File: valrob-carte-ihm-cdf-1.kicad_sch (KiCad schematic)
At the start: 42 parts, among them J1 USB_C_Receptacle_USB2.0_14P, J2 Conn_01x02, J3 Conn_01x02, J4 Conn_01x04_Pin, J5 Conn_01x04_Pin, J9 Conn_01x04_Pin, SW1 SW_Push, SW2 SW_Push, SW3 SW_DIP_x04, U1 TLV75733PDBV, U2 USBLC6-2SC6, U3 ESP32-S3-WROOM-1, U5 HS96L03W2C03

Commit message: schem: connect i2c to MCU
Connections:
- net SCL: now also U3.12 (GPIO8/TOUCH8/ADC1_CH7/SUBSPICS1)
- net SDA: now also U3.17 (GPIO9/TOUCH9/ADC1_CH8/FSPIHD/SUBSPIHD)
- no-connect marks 13 -> 11
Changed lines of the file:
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@@
-	)
-	(no_connect
-		(at 246.38 95.25)
-	)
-	(no_connect
-		(at 246.38 92.71)
 	)
 	(no_connect
@@
 	(wire
 		(pts
+			(xy 250.19 95.25) (xy 246.38 95.25)
+		)
+		(stroke
+			(width 0)
+			(type default)
+		)
+	)
+	(wire
+		(pts
 			(xy 50.8 171.45) (xy 50.8 168.91)
 		)
@@
 	(wire
 		(pts
+			(xy 250.19 92.71) (xy 246.38 92.71)
+		)
+		(stroke
+			(width 0)
+			(type default)
+		)
+	)
+	(wire
+		(pts
 			(xy 200.66 133.35) (xy 200.66 135.89)
 		)
@@
 			(width 0)
 			(type default)
+		)
+	)
+	(label "SDA"
+		(at 250.19 95.25 180)
+		(effects
+			(font
+				(size 1.27 1.27)
+			)
+			(justify right bottom)
 		)
 	)
@@
 		(effects
 			(font
+				(size 1.27 1.27)
+			)
+			(justify right bottom)
+		)
+	)
+	(label "SCL"
+		(at 250.19 92.71 180)
+		(effects
+			(font

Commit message: schem: run and fix ERC
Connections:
- net RGB_LEDS: now also U3.15 (GPIO3/TOUCH3/ADC1_CH2)
- no-connect marks 11 -> 10
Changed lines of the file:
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@@
-	)
-	(no_connect
-		(at 246.38 80.01)
 	)
 	(no_connect
@@
 		(pts
 			(xy 71.12 140.97) (xy 71.12 142.24)
+		)
+		(stroke
+			(width 0)
+			(type default)
+		)
+	)
+	(wire
+		(pts
+			(xy 256.54 80.01) (xy 246.38 80.01)
 		)
 		(stroke
@@
 		(effects
 			(font
+				(size 1.27 1.27)
+			)
+			(justify right bottom)
+		)
+	)
+	(label "RGB_LEDS"
+		(at 256.54 80.01 180)
+		(effects
+			(font

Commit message: schem: add title
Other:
- company: (none) -> Valrobotik
- title: (none) -> Carte IHM CDF 1
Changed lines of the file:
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@@
 	(generator_version "9.0")
 	(paper "A4")
+	(title_block
+		(title "Carte IHM CDF 1")
+		(date "2025-11-24")
+		(rev "01")
+		(company "Valrobotik")
+	)
 	(rectangle
 		(start 15.24 118.11)

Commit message: schem: reannotate
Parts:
- renumbered D12 to D1, D16 to D2, D13 to D3, D1 to D4, D14 to D5, D2 to D6, D3 to D7, D4 to D8, D5 to D9, J9 to J4, J4 to J6, R6 to R5, R5 to R6, TP6 to TP1, TP7 to TP2, U5 to U3, U3 to U4

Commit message: schem: assign footprints
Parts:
- C1, C2: footprint (none) -> Capacitor_SMD:C_0603_1608Metric
- C4: footprint Capacitor_SMD:C_0603_1608Metric -> Capacitor_SMD:C_0402_1005Metric; Basic Y -> (none); JLCPCB Part # C14663 -> (none); Manufacturer YAGEO -> (none); Manufacturer Part Number CC0603KRX7R9BB104 -> (none)
- C5: footprint Capacitor_SMD:C_0603_1608Metric -> Capacitor_SMD:C_0402_1005Metric; JLCPCB Part # C15849 -> (none); Manufacturer Samsung Electro-Mechanics -> (none)
- C6: footprint Capacitor_SMD:C_0805_2012Metric -> Capacitor_SMD:C_0603_1608Metric; Basic Y -> (none); JLCPCB Part # C45783 -> (none); Manufacturer Samsung Electro-Mechanics -> (none); Manufacturer Part Number CL21A226MAQNNNE -> (none)
- C7: footprint Capacitor_SMD:C_0603_1608Metric -> Capacitor_SMD:C_0402_1005Metric; JLCPCB Part # C14663 -> (none); Manufacturer YAGEO -> (none)
- R1, R2, R3: footprint Resistor_SMD:R_0603_1608Metric -> Resistor_SMD:R_0402_1005Metric; JLCPCB Part # C23186 -> (none); Manufacturer Uniroyal Elec -> (none)
- R4: footprint Resistor_SMD:R_0603_1608Metric -> Resistor_SMD:R_0402_1005Metric; JLCPCB Part # C59461 -> (none); Manufacturer Samsung Electro-Mechanics -> (none)
- R5, R6, R7: footprint Resistor_SMD:R_0603_1608Metric -> Resistor_SMD:R_0402_1005Metric; JLCPCB Part # C25804 -> (none); Manufacturer Uniroyal Elec -> (none)
- R8, R9: footprint Resistor_SMD:R_0603_1608Metric -> Resistor_SMD:R_0402_1005Metric; JLCPCB Part # C23345 -> (none); Manufacturer Uniroyal Elec -> (none)
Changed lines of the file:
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@@
 			)
 		)
-		(property "Footprint" "Resistor_SMD:R_0603_1608Metric"
+		(property "Footprint" "Resistor_SMD:R_0402_1005Metric"
 			(at 45.72 170.688 90)
 			(effects
@@
 			)
 		)
-		(property "Manufacturer" "Uniroyal Elec"
+		(property "Manufacturer" ""
 			(at 45.72 168.91 90)
 			(effects
@@
 			)
 		)
-		(property "JLCPCB Part #" "C23186"
+		(property "JLCPCB Part #" ""
 			(at 45.72 168.91 90)
 			(effects
@@
 			)
 		)
-		(property "Footprint" "Resistor_SMD:R_0603_1608Metric"
+		(property "Footprint" "Resistor_SMD:R_0402_1005Metric"
 			(at 259.08 65.532 90)
 			(effects
@@
 			)
 		)
-		(property "JLCPCB Part #" "C23345"
+		(property "JLCPCB Part #" ""
 			(at 259.08 67.31 90)
 			(effects
@@
 			)
 		)
-		(property "Manufacturer" "Uniroyal Elec"
+		(property "Manufacturer" ""
 			(at 259.08 67.31 90)
 			(effects
@@
 			)
 		)
-		(property "Footprint" "Resistor_SMD:R_0603_1608Metric"
+		(property "Footprint" "Resistor_SMD:R_0402_1005Metric"
 			(at 64.77 132.588 90)
 			(effects
@@
 			)
 		)
-		(property "JLCPCB Part #" "C23186"
+		(property "JLCPCB Part #" ""
 			(at 64.77 130.81 90)
 			(effects
@@
 			)
 		)
-		(property "Manufacturer" "Uniroyal Elec"
+		(property "Manufacturer" ""
 			(at 64.77 130.81 90)
 			(effects
@@
 			)
 		)
-		(property "Footprint" ""
+		(property "Footprint" "Capacitor_SMD:C_0603_1608Metric"
 			(at 26.3652 132.08 0)
 			(effects
@@
 			)
 		)
-		(property "Footprint" "Resistor_SMD:R_0603_1608Metric"
+		(property "Footprint" "Resistor_SMD:R_0402_1005Metric"
 			(at 259.08 66.548 90)
 			(effects
@@
 			)
 		)
-		(property "JLCPCB Part #" "C23345"
+		(property "JLCPCB Part #" ""
 			(at 259.08 64.77 90)
 			(effects
@@
 			)
 		)
-		(property "Manufacturer" "Uniroyal Elec"
+		(property "Manufacturer" ""
 			(at 259.08 64.77 90)
 			(effects
@@
 			)
 		)
-		(property "Footprint" "Resistor_SMD:R_0603_1608Metric"
+		(property "Footprint" "Resistor_SMD:R_0402_1005Metric"
 			(at 45.72 168.148 90)
 			(effects
@@
 			)
 		)
-		(property "Manufacturer" "Uniroyal Elec"
+		(property "Manufacturer" ""
 			(at 45.72 166.37 90)
 			(effects
@@
 			)
 		)
-		(property "JLCPCB Part #" "C23186"
+		(property "JLCPCB Part #" ""
 			(at 45.72 166.37 90)
 			(effects
@@
 			)
 		)
-		(property "Footprint" ""
+		(property "Footprint" "Capacitor_SMD:C_0603_1608Metric"
 			(at 56.1848 132.08 0)
 			(effects
@@
 			)
 		)
-		(property "Footprint" "Capacitor_SMD:C_0603_1608Metric"
+		(property "Footprint" "Capacitor_SMD:C_0402_1005Metric"
 			(at 191.4652 44.45 0)
 			(effects
@@
 			)
 		)
-		(property "JLCPCB Part #" "C14663"
+		(property "JLCPCB Part #" ""
 			(at 190.5 40.64 0)
 			(effects
@@
 			)
 		)
-		(property "Manufacturer" "YAGEO"
+		(property "Manufacturer" ""
 			(at 190.5 40.64 0)
 			(effects
@@
 			)
 		)
-		(property "Footprint" "Resistor_SMD:R_0603_1608Metric"
+		(property "Footprint" "Resistor_SMD:R_0402_1005Metric"
 			(at 99.822 147.32 90)
 			(effects
@@
 			)
 		)
-		(property "JLCPCB Part #" "C59461"
+		(property "JLCPCB Part #" ""
 			(at 101.6 147.32 0)
 			(effects
@@
 			)
 		)
-		(property "Manufacturer" "Samsung Electro-Mechanics"
+		(property "Manufacturer" ""
 			(at 101.6 147.32 0)
 			(effects
@@
 			)
 		)
-		(property "Footprint" "Capacitor_SMD:C_0603_1608Metric"
+		(property "Footprint" "Capacitor_SMD:C_0402_1005Metric"
 			(at 140.97 58.1152 0)
 			(effects
@@
 			)
 		)
-		(property "Manufacturer" "Samsung Electro-Mechanics "
+		(property "Manufacturer" ""
 			(at 137.16 57.15 0)
 			(effects
@@
 			)
 		)
-		(property "JLCPCB Part #" "C15849"
+		(property "JLCPCB Part #" ""
 			(at 137.16 57.15 0)
 			(effects
@@
 			)
 		)
-		(property "Footprint" "Resistor_SMD:R_0603_1608Metric"
+		(property "Footprint" "Resistor_SMD:R_0402_1005Metric"
 			(at 257.81 70.612 90)
 			(effects
@@
 			)
 		)
-		(property "Manufacturer" "Uniroyal Elec"
+		(property "Manufacturer" ""
 			(at 257.81 72.39 0)
 			(effects
@@
 			)
 		)
-		(property "JLCPCB Part #" "C25804"
+		(property "JLCPCB Part #" ""
 			(at 257.81 72.39 0)
 			(effects
@@
 			)
 		)
-		(property "Footprint" "Resistor_SMD:R_0603_1608Metric"
+		(property "Footprint" "Resistor_SMD:R_0402_1005Metric"
 			(at 115.57 140.462 90)
 			(effects
@@
 			)
 		)
-		(property "Manufacturer" "Uniroyal Elec"
+		(property "Manufacturer" ""
 			(at 115.57 142.24 0)
 			(effects
@@
 			)
 		)
-		(property "JLCPCB Part #" "C25804"
+		(property "JLCPCB Part #" ""
 			(at 115.57 142.24 0)
 			(effects
@@
 			)
 		)
-		(property "Footprint" "Capacitor_SMD:C_0603_1608Metric"
+		(property "Footprint" "Capacitor_SMD:C_0402_1005Metric"
 			(at 91.7448 151.13 0)
 			(effects
@@
 			)
 		)
-		(property "Basic" "Y"
+		(property "Basic" ""
 			(at 92.71 147.32 0)
 			(effects
@@
 			)
 		)
-		(property "JLCPCB Part #" "C14663"
+		(property "JLCPCB Part #" ""
 			(at 92.71 147.32 0)
 			(effects
@@
 			)
 		)
-		(property "Manufacturer" "YAGEO"
+		(property "Manufacturer" ""
 			(at 92.71 147.32 0)
 			(effects
@@
 			)
 		)
-		(property "Manufacturer Part Number" "CC0603KRX7R9BB104"
+		(property "Manufacturer Part Number" ""
 			(at 92.71 147.32 0)
 			(effects
@@
 			)
 		)
-		(property "Footprint" "Capacitor_SMD:C_0805_2012Metric"
+		(property "Footprint" "Capacitor_SMD:C_0603_1608Metric"
 			(at 181.9148 44.45 0)
 			(effects
@@
 			)
 		)
-		(property "Basic" "Y"
+		(property "Basic" ""
 			(at 182.88 40.64 0)
 			(effects
@@
 			)
 		)
-		(property "JLCPCB Part #" "C45783"
+		(property "JLCPCB Part #" ""
 			(at 182.88 40.64 0)
 			(effects
@@
 			)
 		)
-		(property "Manufacturer" "Samsung Electro-Mechanics "
+		(property "Manufacturer" ""
 			(at 182.88 40.64 0)
 			(effects
@@
 			)
 		)
-		(property "Manufacturer Part Number" "CL21A226MAQNNNE"
+		(property "Manufacturer Part Number" ""
 			(at 182.88 40.64 0)
 			(effects
@@
 			)
 		)
-		(property "Footprint" "Resistor_SMD:R_0603_1608Metric"
+		(property "Footprint" "Resistor_SMD:R_0402_1005Metric"
 			(at 144.018 52.07 90)
 			(effects
@@
 			)
 		)
-		(property "Manufacturer" "Uniroyal Elec"
+		(property "Manufacturer" ""
 			(at 142.24 52.07 0)
 			(effects
@@
 			)
 		)
-		(property "JLCPCB Part #" "C25804"
+		(property "JLCPCB Part #" ""
 			(at 142.24 52.07 0)
 			(effects

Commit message: schem: add part numbers to BOM
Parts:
- C1, C2, C6: Basic (none) -> Y; JLCPCB Part # (none) -> C59461; Manufacturer (none) -> Samsung Electro-Mechanics; Manufacturer Part Number (none) -> CL10A226MQ8NRNC
- C4: Basic (none) -> Y; JLCPCB Part # (none) -> C1525; Manufacturer (none) -> Samsung Electro-Mechanics; Manufacturer Part Number (none) -> CL05B104KO5NNNC
- C5: JLCPCB Part # (none) -> C52923; Manufacturer (none) -> Samsung Electro-Mechanics; Manufacturer Part Number CL10A105KB8NNNC -> CL05A105KA5NQNC
- C7: JLCPCB Part # (none) -> C1525; Manufacturer (none) -> Samsung Electro-Mechanics; Manufacturer Part Number CC0603KRX7R9BB104 -> CL05B104KO5NNNC
- D1, D3, D5: Basic (none) -> X; JLCPCB Part # (none) -> C22371521; Manufacturer (none) -> Worldsemi; Manufacturer Part Number (none) -> WS2812B-HS01/W
- R1, R2, R3: JLCPCB Part # (none) -> C25905; Manufacturer (none) -> Uniroyal Elec; Manufacturer Part Number 0603WAF5101T5E -> 0402WGF5101TCE
- R4: footprint Resistor_SMD:R_0402_1005Metric -> Resistor_SMD:R_0603_1608Metric; JLCPCB Part # (none) -> C4177; Manufacturer (none) -> Uniroyal Elec; Manufacturer Part Number CL10A226MQ8NRNC -> 0603WAF1801T5E
- R5, R6, R7: JLCPCB Part # (none) -> C25744; Manufacturer (none) -> Uniroyal Elec; Manufacturer Part Number 0603WAF1002T5E -> 0402WGF1002TCE
- R8, R9: JLCPCB Part # (none) -> C25092; Manufacturer (none) -> Uniroyal Elec; Manufacturer Part Number 0603WAF220JT5E -> 0402WGF220JTCE
- U1: Basic (none) -> X; JLCPCB Part # (none) -> C485517; Manufacturer (none) -> Texas Instruments; Manufacturer Part Number (none) -> TLV75733PDBVR
- U3: now left out of the parts list

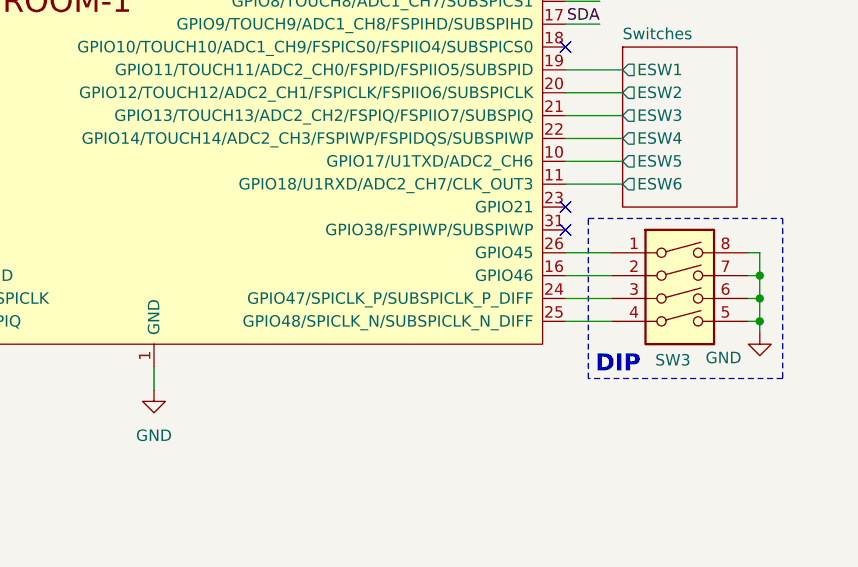
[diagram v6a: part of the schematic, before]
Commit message: pcb: add initial rough placement
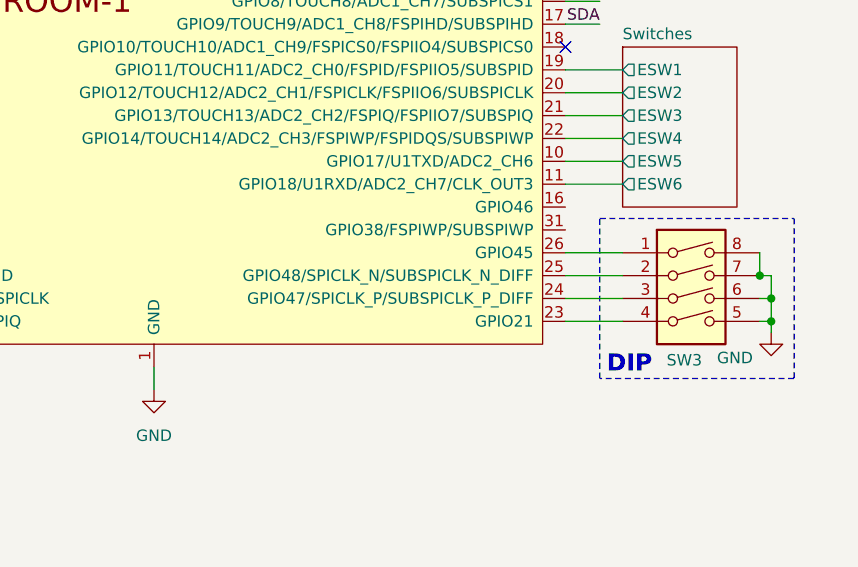
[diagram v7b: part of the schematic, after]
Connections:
- net at U4.16 (GPIO46): no longer SW3.2
- net at U4.23 (GPIO21): now also SW3.4
- net at U4.25 (GPIO48/SPICLK_N/SUBSPICLK_N_DIFF): now also SW3.2; no longer SW3.4
- no-connect marks 10 -> 8
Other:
- moved on the sheet: SW3
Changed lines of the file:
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@@
 	)
 	(rectangle
-		(start 248.92 116.84)
-		(end 270.51 134.62)
+		(start 250.19 116.84)
+		(end 271.78 134.62)
 		(stroke
 			(width 0)
@@
 	(text "DIP"
 		(exclude_from_sim no)
-		(at 252.222 133.096 0)
+		(at 253.492 133.096 0)
 		(effects
 			(font
@@
 	)
 	(junction
-		(at 267.97 128.27)
+		(at 269.24 128.27)
 		(diameter 0)
 		(color 0 0 0 0)
@@
 	)
 	(junction
-		(at 267.97 125.73)
+		(at 269.24 125.73)
 		(diameter 0)
 		(color 0 0 0 0)
@@
 	)
 	(no_connect
-		(at 246.38 118.11)
-	)
-	(no_connect
 		(at 154.94 128.27)
 	)
@@
 		(at 246.38 74.93)
 	)
-	(no_connect
-		(at 246.38 115.57)
-	)
 	(wire
 		(pts
-			(xy 246.38 125.73) (xy 251.46 125.73)
+			(xy 246.38 125.73) (xy 252.73 125.73)
 		)
 		(stroke
@@
 	(wire
 		(pts
-			(xy 267.97 129.54) (xy 267.97 128.27)
+			(xy 269.24 129.54) (xy 269.24 128.27)
 		)
 		(stroke
@@
 	(wire
 		(pts
+			(xy 246.38 120.65) (xy 252.73 120.65)
+		)
+		(stroke
+			(width 0)
+			(type default)
+		)
+	)
+	(wire
+		(pts
 			(xy 53.34 130.81) (xy 57.15 130.81)
 		)
@@
 	(wire
 		(pts
-			(xy 246.38 128.27) (xy 251.46 128.27)
+			(xy 246.38 128.27) (xy 252.73 128.27)
 		)
 		(stroke
@@
 	(wire
 		(pts
+			(xy 269.24 123.19) (xy 267.97 123.19)
+		)
+		(stroke
+			(width 0)
+			(type default)
+		)
+	)
+	(wire
+		(pts
 			(xy 52.07 90.17) (xy 68.58 90.17)
 		)
@@
 	(wire
 		(pts
-			(xy 267.97 125.73) (xy 267.97 128.27)
+			(xy 269.24 125.73) (xy 269.24 128.27)
 		)
 		(stroke
@@
 	(wire
 		(pts
-			(xy 266.7 125.73) (xy 267.97 125.73)
+			(xy 267.97 125.73) (xy 269.24 125.73)
 		)
 		(stroke
@@
 	(wire
 		(pts
-			(xy 246.38 120.65) (xy 251.46 120.65)
-		)
-		(stroke
-			(width 0)
-			(type default)
-		)
-	)
-	(wire
-		(pts
 			(xy 246.38 67.31) (xy 255.27 67.31)
 		)
@@
 	(wire
 		(pts
-			(xy 246.38 123.19) (xy 251.46 123.19)
+			(xy 246.38 123.19) (xy 252.73 123.19)
 		)
 		(stroke
@@
 	(wire
 		(pts
-			(xy 267.97 123.19) (xy 266.7 123.19)
-		)
-		(stroke
-			(width 0)
-			(type default)
-		)
-	)
-	(wire
-		(pts
 			(xy 50.8 176.53) (xy 43.18 176.53)
 		)
@@
 	(wire
 		(pts
-			(xy 267.97 128.27) (xy 266.7 128.27)
+			(xy 269.24 128.27) (xy 267.97 128.27)
 		)
 		(stroke
@@
 	(wire
 		(pts
-			(xy 267.97 125.73) (xy 267.97 123.19)
+			(xy 269.24 125.73) (xy 269.24 123.19)
 		)
 		(stroke
@@
 	(wire
 		(pts
-			(xy 267.97 120.65) (xy 266.7 120.65)
-		)
-		(stroke
-			(width 0)
-			(type default)
-		)
-	)
-	(wire
-		(pts
 			(xy 31.75 133.35) (xy 29.21 133.35)
 		)
@@
 	(symbol
 		(lib_id "Switch:SW_DIP_x04")
-		(at 259.08 125.73 0)
+		(at 260.35 125.73 0)
 		(unit 1)
 		(exclude_from_sim no)
@@
 		(dnp no)
 		(property "Reference" "SW3"
-			(at 258.318 132.588 0)
+			(at 259.588 132.588 0)
 			(effects
 				(font
@@
 		)
 		(property "Value" "SW_DIP_x04"
-			(at 258.572 116.84 0)
+			(at 259.842 116.84 0)
 			(effects
 				(font
@@
 		)
 		(property "Footprint" "Button_Switch_THT:SW_DIP_SPSTx04_Slide_9.78x12.34mm_W7.62mm_P2.54mm"
-			(at 259.08 125.73 0)
+			(at 260.35 125.73 0)
 			(effects
 				(font
@@
 		)
 		(property "Datasheet" "~"
-			(at 259.08 125.73 0)
+			(at 260.35 125.73 0)
 			(effects
 				(font
@@
 		)
 		(property "Description" "4x DIP Switch, Single Pole Single Throw (SPST) switch, small symbol"
-			(at 259.08 125.73 0)
+			(at 260.35 125.73 0)
 			(effects
 				(font
@@
 		)
 		(property "Manufacturer" ""
-			(at 259.08 125.73 0)
+			(at 260.35 125.73 0)
 			(effects
 				(font
@@
 		)
 		(property "Manufacturer Part Number" ""
-			(at 259.08 125.73 0)
+			(at 260.35 125.73 0)
 			(effects
 				(font
@@
 		)
 		(property "Basic" ""
-			(at 259.08 125.73 0)
+			(at 260.35 125.73 0)
 			(effects
 				(font
@@
 	(symbol
 		(lib_id "power:GND")
-		(at 267.97 129.54 0)
+		(at 269.24 129.54 0)
 		(unit 1)
 		(exclude_from_sim no)
@@
 		(dnp no)
 		(property "Reference" "#PWR033"
-			(at 267.97 135.89 0)
+			(at 269.24 135.89 0)
 			(effects
 				(font
@@
 		)
 		(property "Value" "GND"
-			(at 265.938 132.334 0)
+			(at 267.208 132.334 0)
 			(effects
 				(font
@@
 		)
 		(property "Footprint" ""
-			(at 267.97 129.54 0)
+			(at 269.24 129.54 0)
 			(effects
 				(font
@@
 		)
 		(property "Datasheet" ""
-			(at 267.97 129.54 0)
+			(at 269.24 129.54 0)
 			(effects
 				(font
@@
 		)
 		(property "Description" "Power symbol creates a global label with name \"GND\" , ground"
-			(at 267.97 129.54 0)
+			(at 269.24 129.54 0)
 			(effects
 				(font

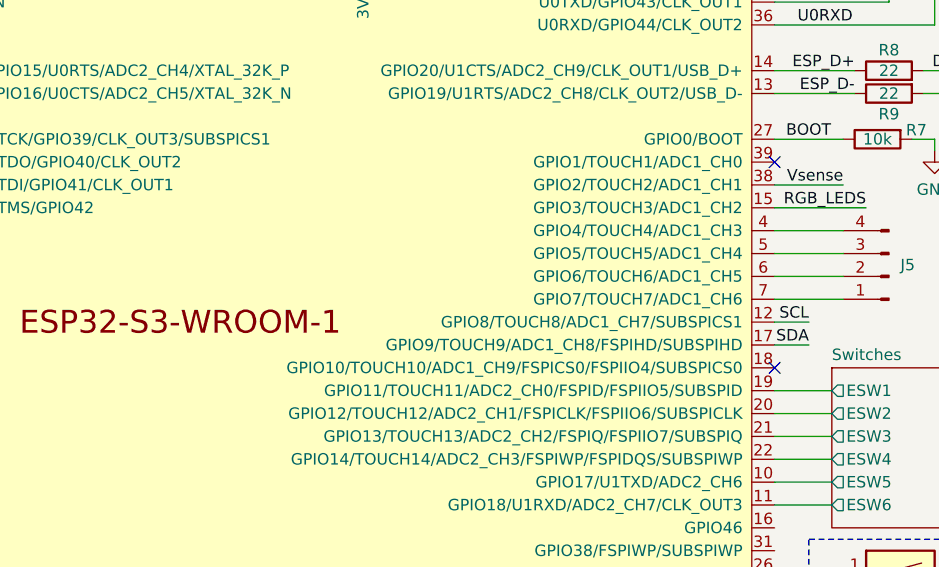
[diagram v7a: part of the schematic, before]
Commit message: pcb: add UART routing
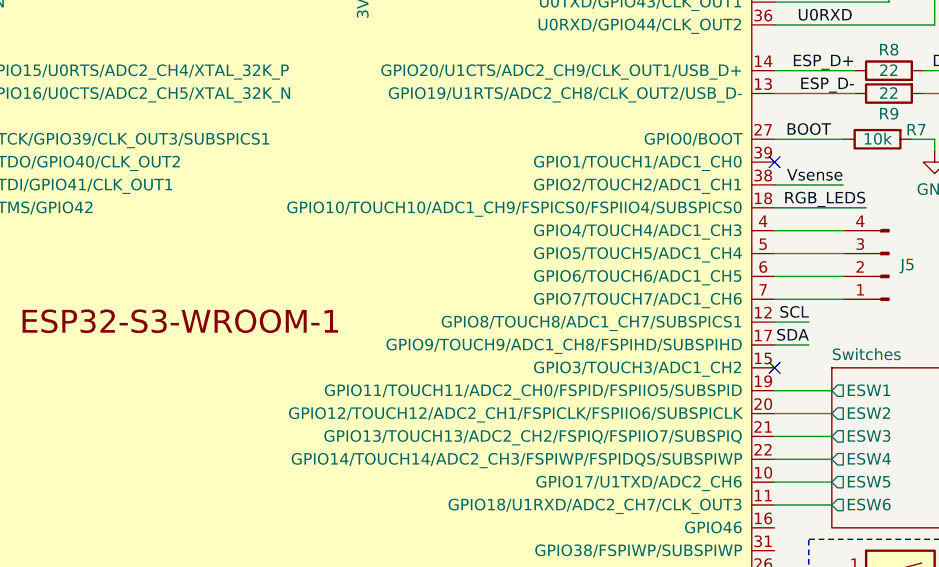
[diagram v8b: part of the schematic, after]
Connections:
- net RGB_LEDS: now also U4.18 (GPIO10/TOUCH10/ADC1_CH9/FSPICS0/FSPIIO4/SUBSPICS0); no longer U4.15 (GPIO3/TOUCH3/ADC1_CH2)
